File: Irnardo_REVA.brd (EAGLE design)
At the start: 100 x 80 mm, 21 parts, among them U1 ATMEGA32U4-MU, U2 TSOP755, X1 16MHz

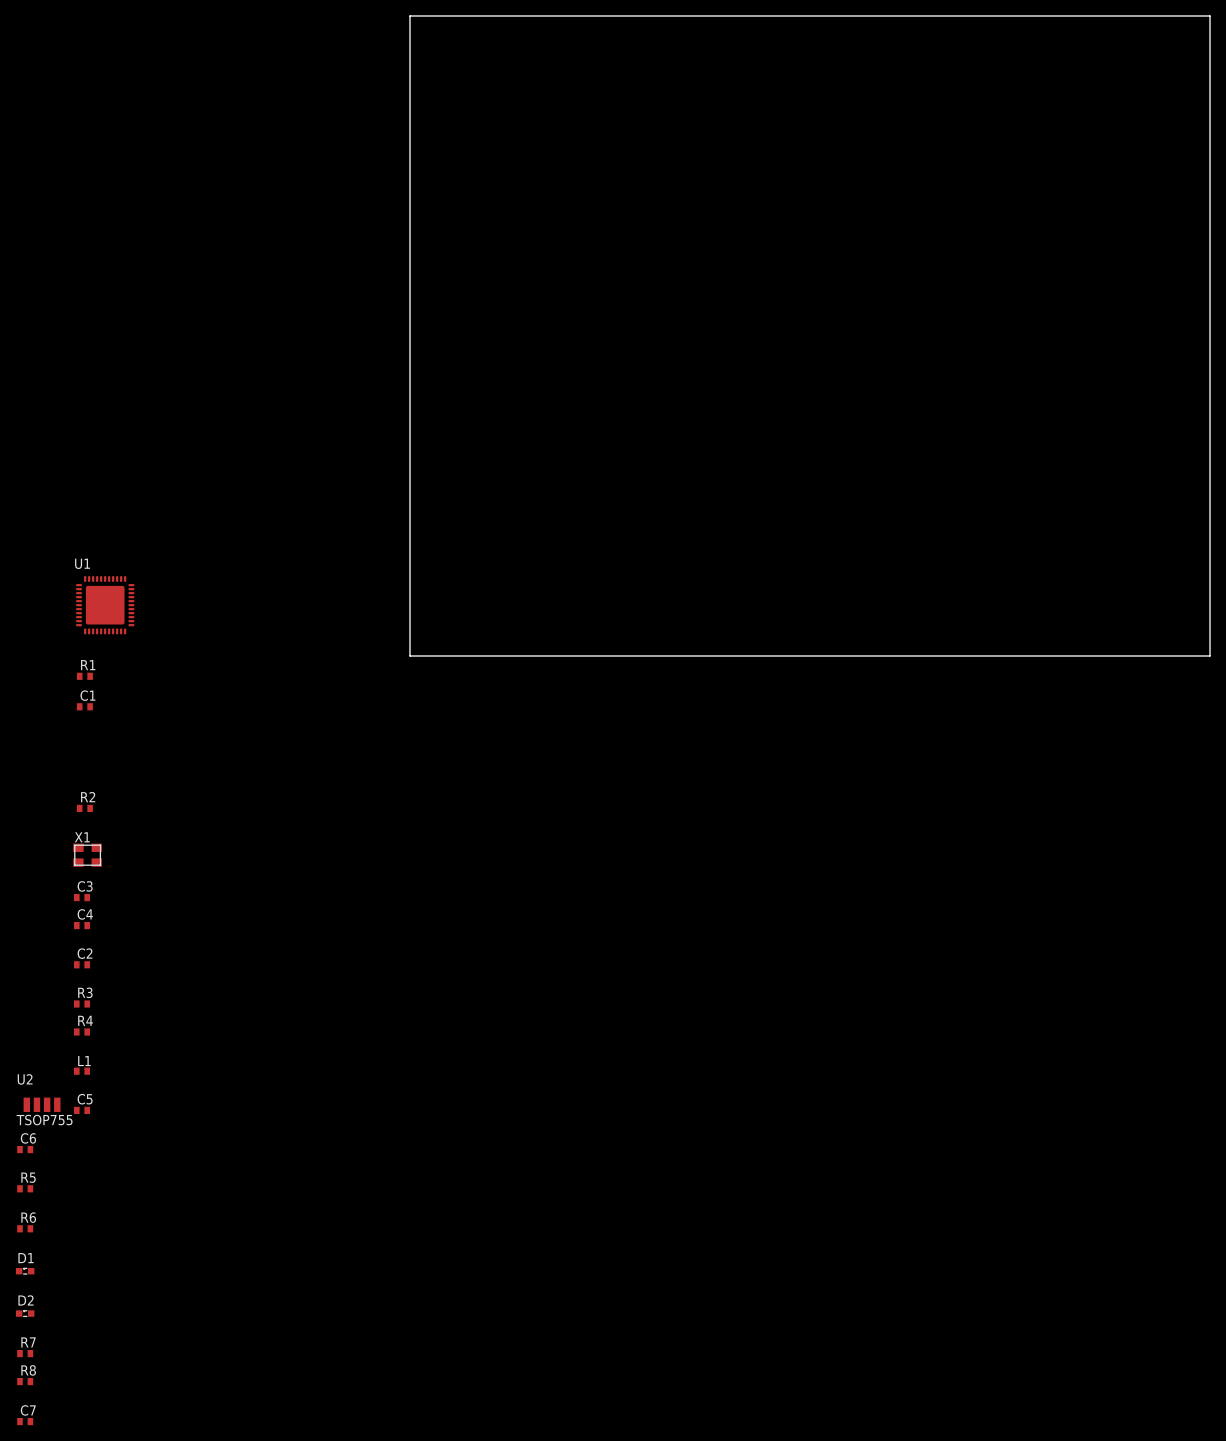
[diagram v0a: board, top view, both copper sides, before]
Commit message: Initial PCB design for DIY etching - incomplete
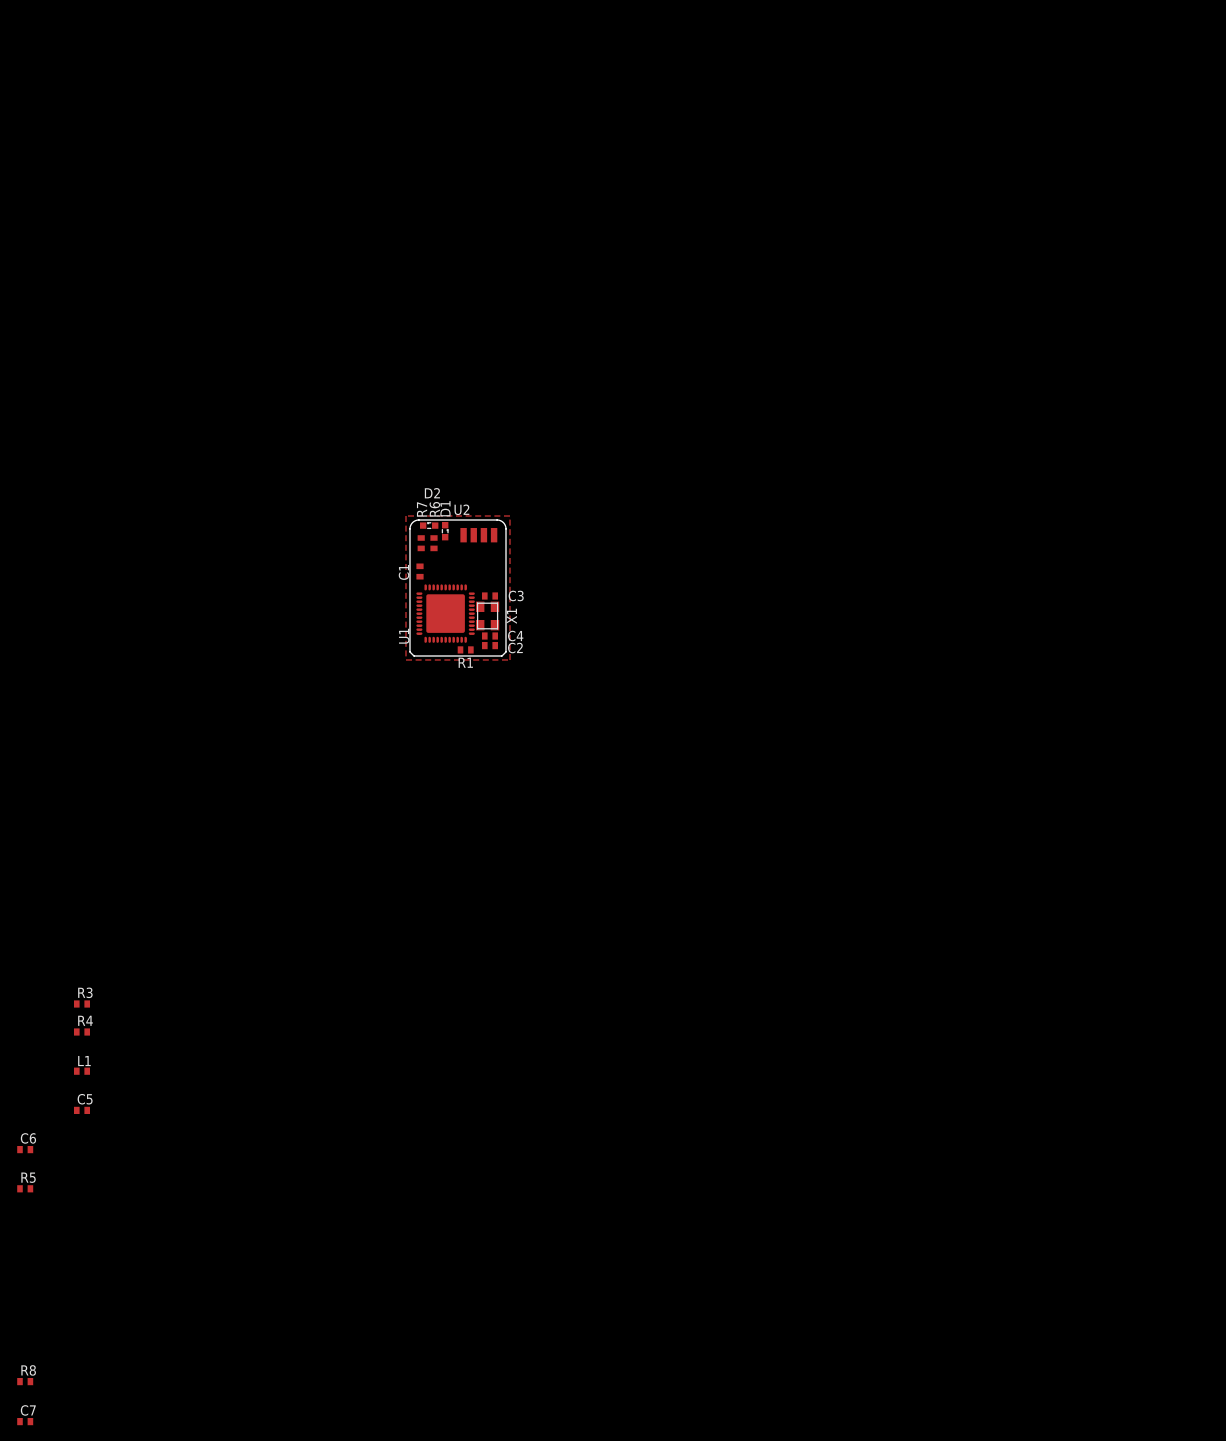
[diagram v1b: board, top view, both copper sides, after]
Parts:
- removed R2: 10M, resistor:R0402
- moved R7 112.7 mm to (1.40, 14.1), turned to 90 degrees
- moved D2 110.7 mm to (2.40, 16.3)
- moved D1 106.4 mm to (4.40, 15.6), turned to 270 degrees
- moved R6 99.8 mm to (3.00, 14.1), turned to 90 degrees
- moved U2 89.7 mm to (6.70, 15.1)
- moved C2 64.8 mm to (10.0, 1.30)
- moved C3 63.4 mm to (10.0, 7.50), turned to 180 degrees
- moved C4 62.5 mm to (10.0, 2.50)
- moved X1 58.3 mm to (9.70, 5.00), turned to 270 degrees
- moved R1 47.7 mm to (6.96, 0.76)
- moved C1 45.2 mm to (1.25, 10.6), turned to 90 degrees
- moved U1 42.6 mm to (4.45, 5.30), turned to 90 degrees
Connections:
- net N$1: no longer R2.1
- net N$2: no longer R2.2
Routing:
- added copper zone on layer 1, net GND
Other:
- board size 100 x 80 mm -> 12 x 17 mm

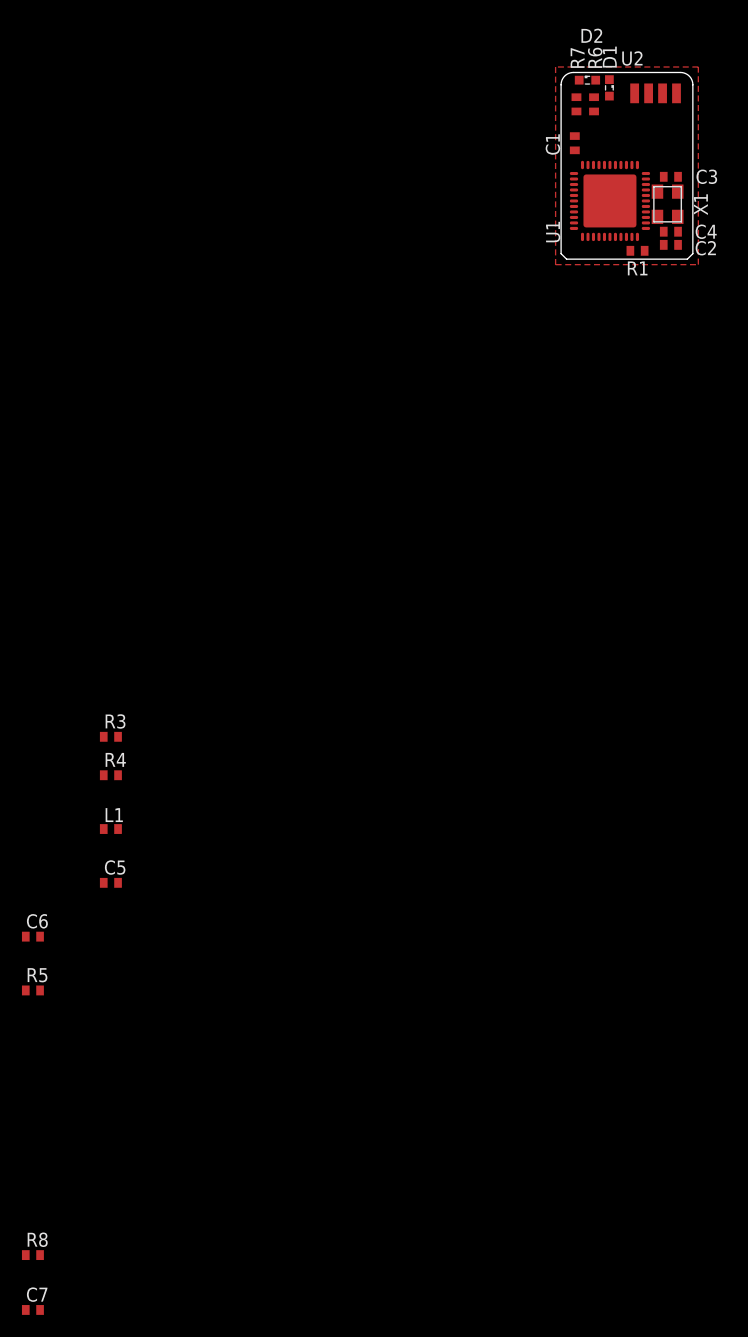
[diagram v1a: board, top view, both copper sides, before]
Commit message: Finished placing and stated wiring REVA
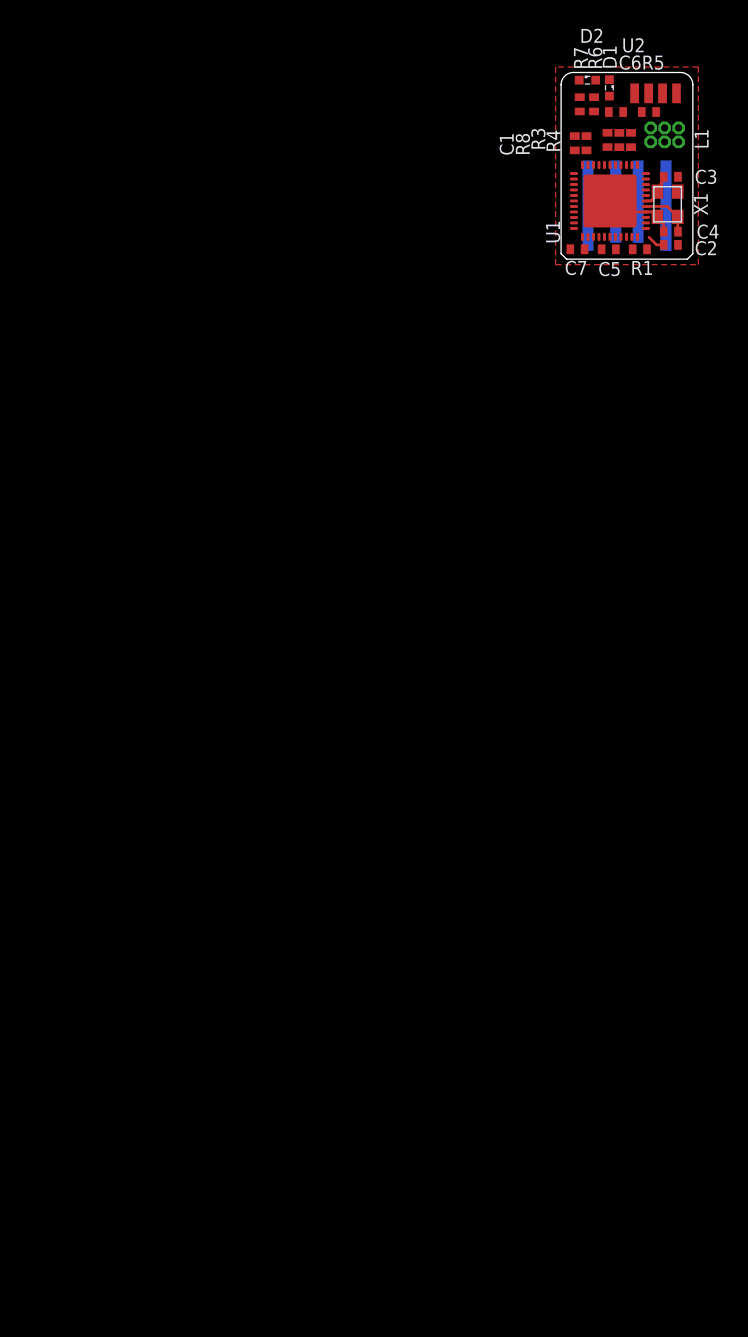
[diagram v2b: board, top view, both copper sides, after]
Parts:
- added J1: ICSP, 6X2005IN:6X2005IN
- moved R8 113.1 mm to (2.31, 10.6), turned to 90 degrees
- moved C7 108.6 mm to (1.49, 0.90), turned to 180 degrees
- moved R5 97.7 mm to (8.00, 13.4), turned to 180 degrees
- moved C6 92.0 mm to (5.00, 13.4), turned to 180 degrees
- moved L1 78.6 mm to (6.37, 10.8), turned to 90 degrees
- moved R4 74.1 mm to (5.30, 10.8), turned to 90 degrees
- moved C5 73.4 mm to (4.34, 0.90), turned to 180 degrees
- moved R3 70.7 mm to (4.23, 10.9), turned to 270 degrees
- moved R7 0.30 mm to (1.70, 14.1)
- moved R1 0.25 mm to (7.17, 0.90)
- turned C3 to 0 degrees
- turned C4 to 180 degrees
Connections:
- removed net N$3: R1.2, U1.13
- removed net N$4: C4.1, X1.2
- removed net N$6: C3.1, X1.4
- new net MISO: J1.1, U1.11
- new net MOSI: J1.4, U1.10
- new net RESET: J1.5, R1.2, U1.13
- new net SCK: J1.3, U1.9
- net +5V: now also J1.2
- net GND: now also J1.6, X1.2, X1.4
- net N$1: now also C3.1
- net N$2: now also C4.1
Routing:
- net GND: track 0.00 -> 6.51 mm
- net N$2: track 0.00 -> 4.65 mm
- net N$1: track 0.00 -> 3.15 mm
- net +5V: track 0.00 -> 1.64 mm

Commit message: First complete(ish) layout.
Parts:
- removed R8: 10K, resistor:R0402
- J1: value ICSP -> USB_PAD; device 6X2005IN:6X2005IN -> USB_PAD:USB_PAD
- moved C7 14.0 mm to (11.1, 11.1), turned to 90 degrees
- moved C1 13.5 mm to (10.5, 0.71), turned to 180 degrees
- moved J1 11.2 mm to (6.00, 0.00), flipped to the bottom
- moved C5 11.1 mm to (6.18, 11.9), turned to 90 degrees
- moved R1 10.5 mm to (3.76, 10.8), turned to 270 degrees
- moved C3 9.93 mm to (1.99, 1.63), turned to 180 degrees
- moved C2 9.72 mm to (2.99, 8.03), turned to 270 degrees
- moved C4 9.68 mm to (1.27, 6.68)
- moved R6 8.39 mm to (11.3, 14.9)
- moved X1 8.04 mm to (1.71, 4.14), turned to 90 degrees
- moved R7 6.21 mm to (7.83, 15.1), turned to 0 degrees
- moved D1 5.87 mm to (10.2, 16.4), turned to 0 degrees
- moved R3 5.78 mm to (9.96, 11.6)
- moved R5 5.55 mm to (2.54, 12.4), turned to 90 degrees
- moved U2 5.35 mm to (1.35, 15.2)
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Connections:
- removed net N$9: R8.1, U1.33
- net +5V: now also J1.V+; no longer J1.2
- net D+: now also J1.D+
- net D-: now also J1.D-
- net GND: now also U1.33; no longer J1.6, R8.2
- net MISO: no longer J1.1
- net MOSI: no longer J1.4
- net RESET: no longer J1.5
- net SCK: no longer J1.3
- net UGND: now also J1.V-
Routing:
- net GND: track 6.51 -> 50.1 mm, vias 0 -> 4
- net +5V: track 1.64 -> 42.3 mm, vias 0 -> 4
- net IO5: track 0.00 -> 23.2 mm, vias 0 -> 2
- net IO8: track 0.00 -> 18.6 mm, vias 0 -> 2
- net IO13: track 0.00 -> 14.1 mm, vias 0 -> 2
- net D-: track 0.00 -> 12.3 mm, vias 0 -> 1
- net UGND: track 0.00 -> 11.5 mm, vias 0 -> 1
- net D+: track 0.00 -> 10.7 mm, vias 0 -> 1
- net UCAP: track 0.00 -> 3.03 mm
- net RESET: track 0.00 -> 2.81 mm
- net N$1: track 3.15 -> 5.67 mm
- net N$5: track 0.00 -> 2.12 mm
- net RD-: track 0.00 -> 1.78 mm
- net RD+: track 0.00 -> 1.74 mm
- net N$7: track 0.00 -> 1.36 mm
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
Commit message: Tweaks to get closer to DRC pass
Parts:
- moved R6 0.22 mm to (11.2, 14.7)
- moved D1 0.10 mm to (10.2, 16.3)
- moved D2 0.10 mm to (7.69, 16.3)
- moved R3 0.05 mm to (9.96, 11.7)
- moved R4 0.05 mm to (8.81, 11.6)
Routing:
- net +5V: track 42.3 -> 26.9 mm, vias 4 -> 3
- net IO13: track 14.1 -> 14.7 mm

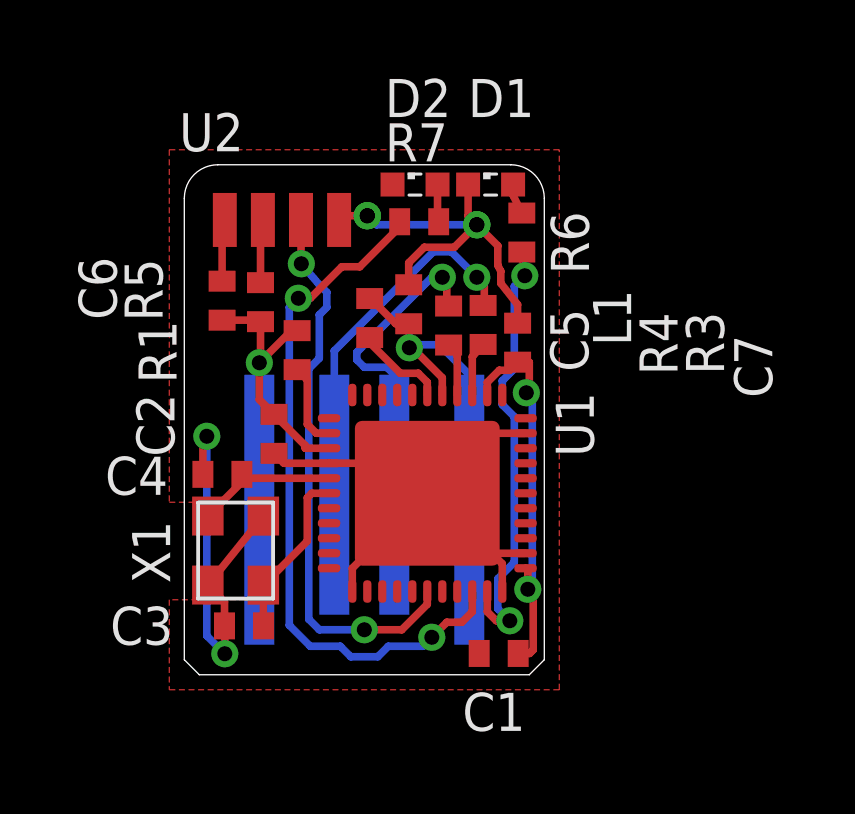
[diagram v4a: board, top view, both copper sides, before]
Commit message: Fixes at hackerspace after printing and talking to
Joel.
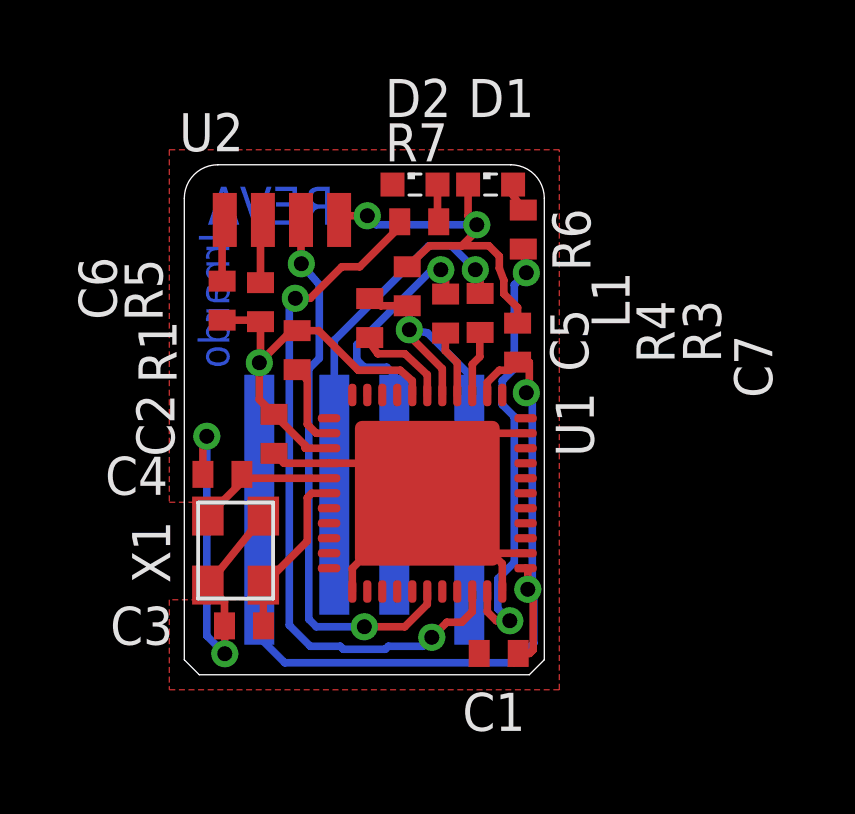
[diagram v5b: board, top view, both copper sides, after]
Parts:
- moved L1 0.60 mm to (7.43, 12.9)
- moved R3 0.41 mm to (9.86, 12.1)
- moved R4 0.41 mm to (8.71, 12.0)
- moved R6 0.11 mm to (11.3, 14.8)
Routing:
- net +5V: track 26.9 -> 47.7 mm
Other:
- board text added: "Irnardo"
- board text added: "REVA"
